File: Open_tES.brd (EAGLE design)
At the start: 105.2 x 98 mm, 58 parts, among them IC2 MAX232ECWES, IC3 4023D, IC4 LP2950CZ-5.0, IC5 OPA277U, IC6 LF444CM, IC7 PIC16F1937P, U1 TSR_1-2465, U2 ICL7660ACPAZ, X1 22-23-2041, X2 057-016-1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

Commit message: replace TSR on the shematic by MIC2288 boost DC-DC
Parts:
- removed C_TSR1, C_TSR2: 22µF, rcl:C1206
- added C1_MIC, C2_MIC: 4.7µF, rcl:C0805
- added D1_MIC: SCHOTTKY, Open_tES:SOD80
- added L_MIC: 10uH, rcl:L2012C
- added R1_MIC: 28.7KR, rcl:R0805
- added R2_MIC: 1.24KR, rcl:R0805
- U1: value TSR_1-2465 -> MIC2288YD5-TR; device _traco_tsr-1:TSR-1 -> Open_tES:SOT23-5L
- moved U1 127.1 mm to (-8.26, -13.3)
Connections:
- removed net +7V: C_ICL2.+, C_ICL4.+, C_LPO1.+, C_TSR2.1, IC4.3, R11.1, SP1.+, U1.3, U2.8
- new net +9V: C2_MIC.1, C_ICL2.+, C_ICL4.+, C_LPO1.+, D1_MIC.C, IC4.3, R11.1, R1_MIC.2, SP1.+, U2.8
- new net N$10: R1_MIC.1, R2_MIC.2, U1.3
- new net N$35: D1_MIC.A, L_MIC.2, U1.1
- net +24V: now also C1_MIC.1, L_MIC.1, U1.4, U1.5; no longer C_TSR1.1, U1.1
- net GND: now also C1_MIC.2, C2_MIC.2, R2_MIC.1; no longer C_TSR1.2, C_TSR2.2
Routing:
- net +7V: track 193.9 -> 0.00 mm
- net +9V: track 0.00 -> 190.2 mm
- net +24V: track 99.5 -> 90.4 mm
- net GND: track 147.4 -> 141.4 mm

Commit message: backlight resistor for 9V supply
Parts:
- R11: value 330 -> 620
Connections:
- net +5V/1: now also C_ICL2.+, U2.8
- net +9V: no longer C_ICL2.+, U2.8
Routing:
- net +9V: track 190.2 -> 175.2 mm
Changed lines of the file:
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@@
 <attribute name="OC_FARNELL" value="8395934" x="5.08" y="15.24" size="1.778" layer="28" rot="MR90" display="off"/>
 </element>
-<element name="R11" library="rcl" package="0204/7" value="330" x="11.43" y="29.845" rot="R270">
-<attribute name="OC_FARNELL" value="9339418" x="11.43" y="29.845" size="1.778" layer="27" rot="R270" display="off"/>
+<element name="R11" library="rcl" package="0204/7" value="620" x="11.43" y="29.845" rot="R270">
+<attribute name="OC_FARNELL" value="2329960" x="11.43" y="29.845" size="1.778" layer="27" rot="R270" display="off"/>
 </element>
 <element name="R1" library="rcl" package="M1406" value="12K" x="33.655" y="62.5475" rot="R180">
@@
 <wire x1="50.8" y1="19.685" x2="51.5925" y2="20.4775" width="0.6096" layer="16"/>
 <wire x1="45.72" y1="29.845" x2="45.72" y2="32.0675" width="1.27" layer="1"/>
+<contactref element="U2" pad="8"/>
+<contactref element="C_ICL2" pad="+"/>
+<wire x1="85.09" y1="52.705" x2="91.44" y2="64.516" width="0" layer="19" extent="1-1"/>
+<wire x1="97.79" y1="52.705" x2="85.09" y2="52.705" width="0" layer="19" extent="1-1"/>
 <wire x1="45.72" y1="29.845" x2="45.72" y2="30.48" width="0" layer="19" extent="1-16"/>
 </signal>
@@
 <wire x1="93.091" y1="50.546" x2="95.25" y2="52.705" width="1.27" layer="16"/>
 <contactref element="R11" pad="1"/>
-<contactref element="U2" pad="8"/>
-<contactref element="C_ICL2" pad="+"/>
 <wire x1="83.82" y1="72.705" x2="90.675" y2="73.155" width="1.27" layer="16"/>
 <wire x1="90.675" y1="73.155" x2="93.98" y2="69.85" width="1.27" layer="16"/>
 <wire x1="93.98" y1="69.85" x2="93.98" y2="65.405" width="1.27" layer="16"/>
-<wire x1="91.44" y1="64.516" x2="93.091" y2="64.516" width="1.27" layer="16"/>
 <wire x1="93.091" y1="64.516" x2="93.98" y2="65.405" width="1.27" layer="16"/>
 <contactref element="SP1" pad="+"/>
@@
 <wire x1="63.4365" y1="2.4765" x2="63.4365" y2="11.7475" width="1.27" layer="16"/>
 <wire x1="95.25" y1="52.705" x2="95.25" y2="60.706" width="1.27" layer="16"/>
-<wire x1="95.25" y1="60.706" x2="91.44" y2="64.516" width="1.27" layer="16"/>
-<wire x1="85.09" y1="52.705" x2="90.551" y2="52.705" width="1.27" layer="16"/>
 <wire x1="90.551" y1="52.705" x2="93.091" y2="50.165" width="1.27" layer="16"/>
-<wire x1="85.09" y1="52.705" x2="85.09" y2="50.165" width="1.27" layer="1"/>
 <wire x1="85.09" y1="50.165" x2="78.105" y2="43.18" width="1.27" layer="1"/>
 <wire x1="78.105" y1="43.18" x2="78.105" y2="23.495" width="1.27" layer="1"/>
@@
 <contactref element="R1_MIC" pad="2"/>
 <contactref element="D1_MIC" pad="C"/>
-<wire x1="-7.305" y1="-24.765" x2="-9.905" y2="-35.56" width="0" layer="19" extent="1-1"/>
-<wire x1="15.875" y1="22.225" x2="-7.305" y2="-24.765" width="0" layer="19" extent="1-1"/>
+<wire x1="95.25" y1="60.706" x2="93.091" y2="64.516" width="0" layer="19" extent="16-16"/>
+<wire x1="85.09" y1="50.165" x2="90.551" y2="52.705" width="0" layer="19" extent="1-16"/>
+<wire x1="-7.305" y1="-24.765" x2="15.875" y2="22.225" width="0" layer="19" extent="1-1"/>
+<wire x1="-9.905" y1="-35.56" x2="-7.305" y2="-24.765" width="0" layer="19" extent="1-1"/>
 </signal>
 <signal name="N$21">

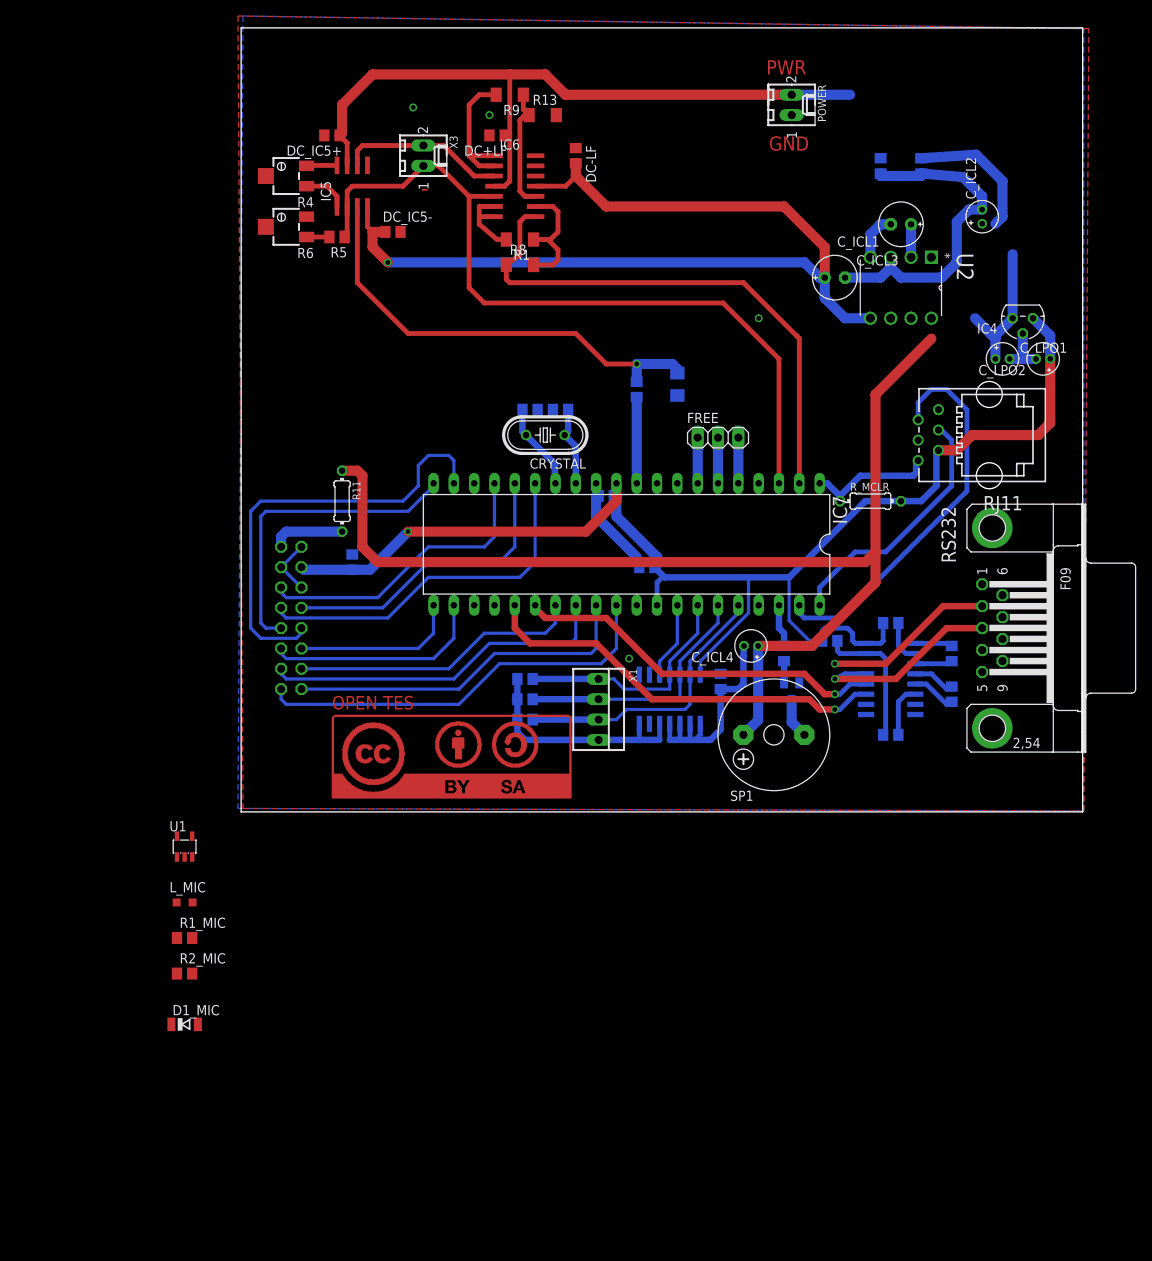
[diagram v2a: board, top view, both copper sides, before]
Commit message: use of MAX232 for negative voltage with MIC5270 for regulation (-5V)
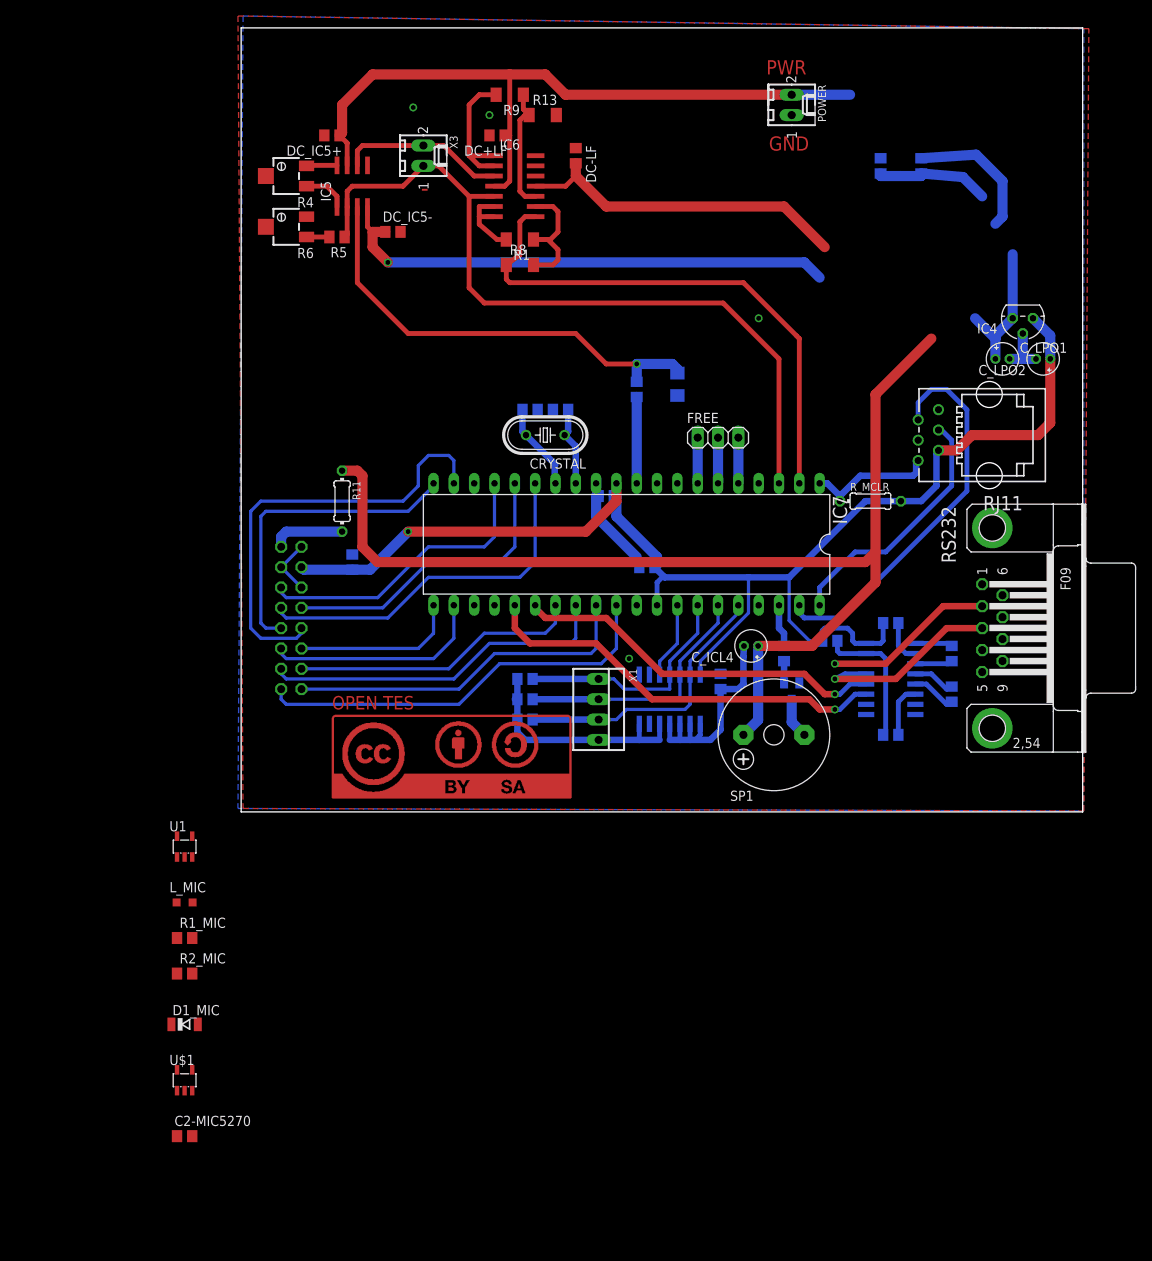
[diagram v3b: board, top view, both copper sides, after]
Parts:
- removed C_ICL1, C_ICL3: 100µF, rcl:E2,5-6E
- removed C_ICL2: 2.2µF, rcl:E1,8-4
- removed U2: ICL7660ACPAZ, Intersil-ICL7660:DIP254P762X533-8
- added C2-MIC5270: 10µF, rcl:C0805
- added U$1: MIC5270, Open_tES:SOT23-5L
- C1+-, C2+-, CV+, CV-: value 0.1µF -> 1µF
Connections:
- removed net N$21: C_ICL1.+, U2.2
- removed net N$27: C_ICL1.-, U2.4
- removed net N$33: CV-.1, IC2.6
- new net V-MAX232: CV-.1, IC2.6, U$1.5
- net +5V/1: no longer C_ICL2.+, U2.8
- net -5V: now also C2-MIC5270.2, U$1.4; no longer C_ICL3.+, U2.5
- net GND: now also C2-MIC5270.1, U$1.2; no longer C_ICL2.-, C_ICL3.-, U2.1, U2.3
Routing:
- net GND: track 141.4 -> 113.8 mm
- net -5V: track 120.0 -> 106.3 mm
- net V-MAX232: track 0.00 -> 6.64 mm
- net N$33: track 6.64 -> 0.00 mm
- net N$27: track 5.92 -> 0.00 mm
- net N$21: track 4.13 -> 0.00 mm

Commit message: 1)replace 4023 triple 3-input NAND with 74LVC1G10W6-7 simple 3-input NAND 2) solve consistent problem between sch and brd
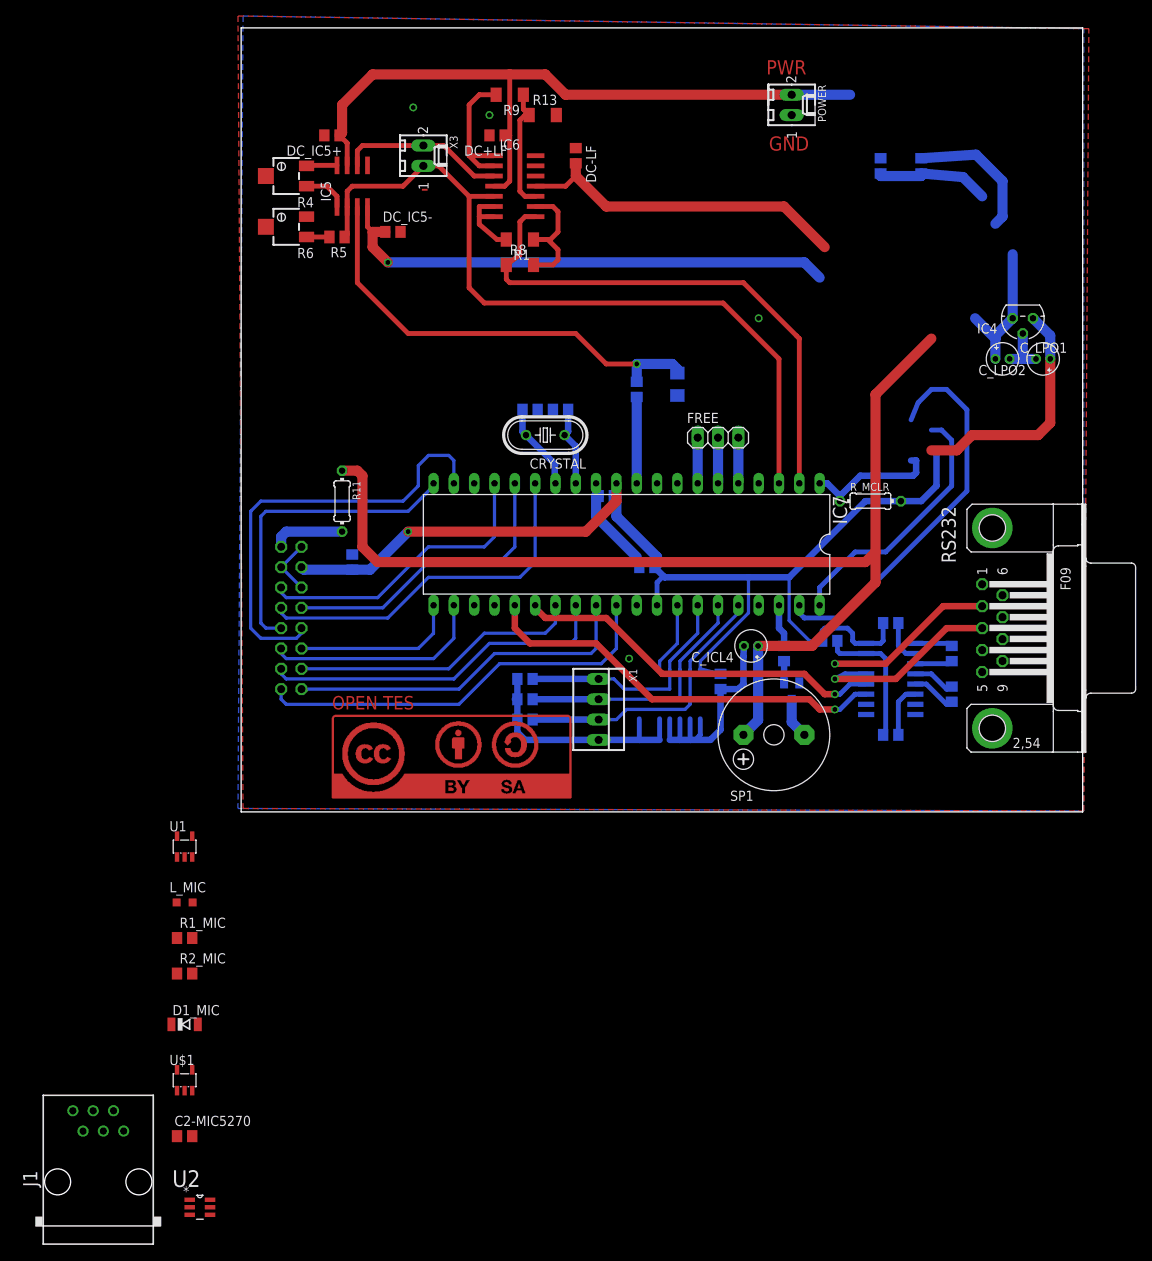
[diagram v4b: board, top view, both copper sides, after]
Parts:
- removed IC3: 4023D, 40xx:SO14
- removed RJ11: (no value), con-amp:520425-3
- added J1: RJ11-2X, con-tycoelectronics:RJ11-NO_SHIELD
- added U2: 74LVC1G10W6-7, Open_tES:SOT95P280X135-6N
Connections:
- net +5V/1: now also J1.2, U2.5; no longer IC3.14, RJ11.2
- net GND: now also J1.3, U2.2; no longer IC3.1, IC3.2, IC3.3, IC3.4, IC3.5, IC3.7, IC3.8, RJ11.3
- net MCLR: now also J1.1; no longer RJ11.1
- net N$18: now also U2.6; no longer IC3.13
- net N$23: now also U2.3; no longer IC3.12
- net N$25: now also U2.4; no longer IC3.10
- net N$9: now also U2.1; no longer IC3.11
- net PGC: now also J1.5; no longer RJ11.5
- net PGD: now also J1.4; no longer RJ11.4
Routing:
- net GND: track 113.8 -> 117.6 mm
- net PGD: track 31.9 -> 32.8 mm
- net N$25: track 9.59 -> 8.96 mm
- net +5V/1: track 175.6 -> 176.3 mm
